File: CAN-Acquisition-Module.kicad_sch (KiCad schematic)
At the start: 0 parts

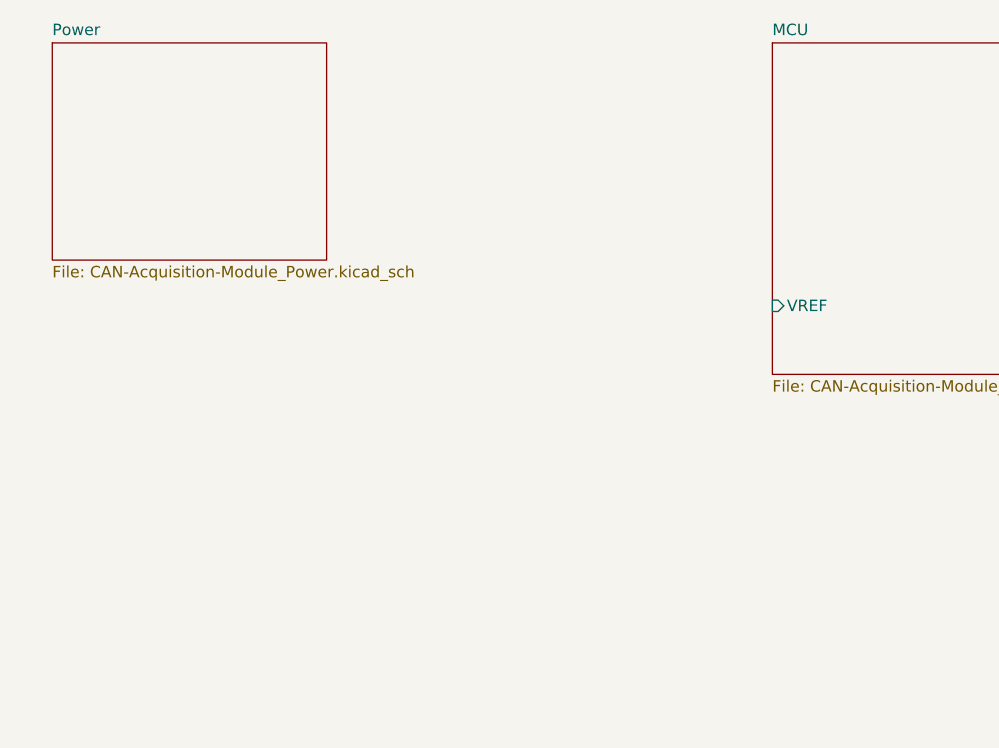
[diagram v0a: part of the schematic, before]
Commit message: Added CAN page
also power section has advanced
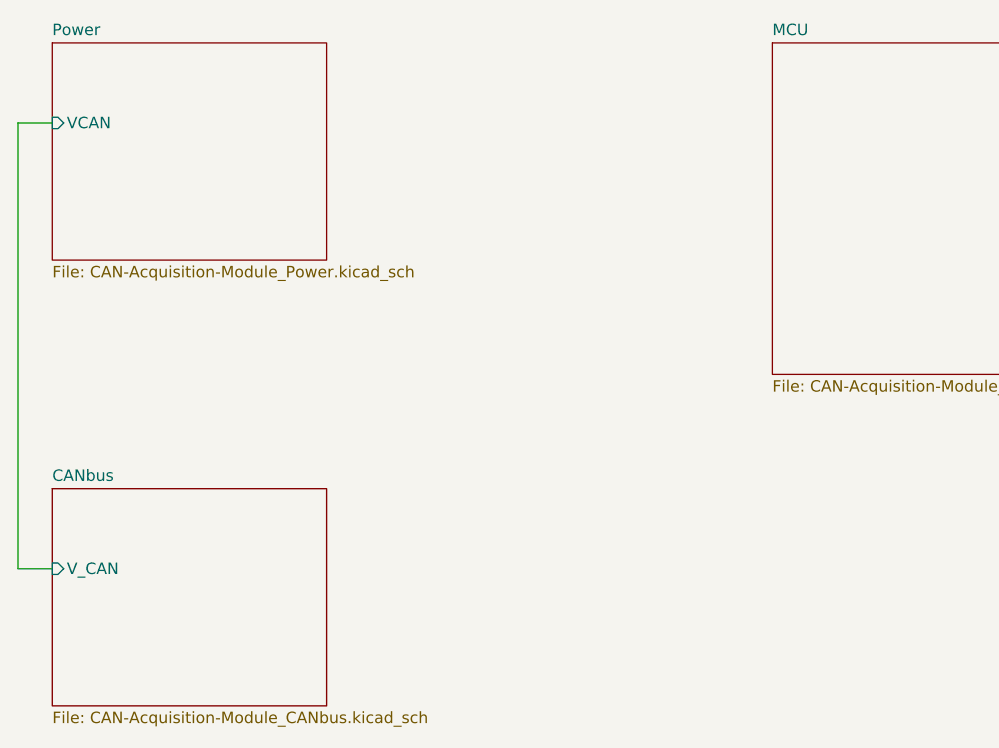
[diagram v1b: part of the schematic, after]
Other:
- added sheet CANbus (CAN-Acquisition-Module_CANbus.kicad_sch)
- sheet MCU ports: added none; removed VREF
- sheet Power ports: added VCAN; removed none

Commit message: Mid-day backup
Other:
- sheet MCU ports: added V_USB; removed none
- sheet Power ports: added V_CAN, V_USB; removed VCAN
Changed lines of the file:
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@@
 (kicad_sch (version 20211123) (generator eeschema)
   (paper "A4")
+  (wire (pts (xy 123.19 48.26) (xy 96.52 48.26))
+    (stroke (width 0) (type default) (color 0 0 0 0))
+  )
   (wire (pts (xy 39.37 101.6) (xy 43.18 101.6))
     (stroke (width 0) (type default) (color 0 0 0 0))
   )
   (wire (pts (xy 43.18 52.07) (xy 39.37 52.07))
+    (stroke (width 0) (type default) (color 0 0 0 0))
+  )
+  (wire (pts (xy 96.52 46.99) (xy 73.66 46.99))
+    (stroke (width 0) (type default) (color 0 0 0 0))
+  )
+  (wire (pts (xy 96.52 48.26) (xy 96.52 46.99))
     (stroke (width 0) (type default) (color 0 0 0 0))
   )
@@
       (effects (font (size 1.27 1.27)) (justify left top))
     )
+    (pin "V_USB" input (at 123.19 48.26 180)
+      (effects (font (size 1.27 1.27)) (justify left))
+    )
   )
   (sheet (at 43.18 43.18) (size 30.48 24.13) (fields_autoplaced)
@@
       (effects (font (size 1.27 1.27)) (justify left top))
     )
-    (pin "VCAN" input (at 43.18 52.07 180)
+    (pin "V_CAN" input (at 43.18 52.07 180)
       (effects (font (size 1.27 1.27)) (justify left))
+    )
+    (pin "V_USB" input (at 73.66 46.99 0)
+      (effects (font (size 1.27 1.27)) (justify right))
     )
   )
@@
       (reference "#PWR?") (unit 1) (value "+3.3VA") (footprint "")
     )
+    (path "/00000000-0000-0000-0000-0000628fa103/a38a5452-85ed-4430-a87b-bb057f60819d"
+      (reference "#PWR?") (unit 1) (value "GND") (footprint "")
+    )
     (path "/00000000-0000-0000-0000-0000628fba98/a44a161f-59e8-4a07-bda9-a9f7ef5f0a45"
+      (reference "#PWR?") (unit 1) (value "GND") (footprint "")
+    )
+    (path "/00000000-0000-0000-0000-0000628fa103/b9203d8f-14b0-4cbc-9d0d-c6be62782233"
       (reference "#PWR?") (unit 1) (value "GND") (footprint "")
     )
@@
       (reference "J?") (unit 1) (value "Conn_01x04") (footprint "")
     )
+    (path "/00000000-0000-0000-0000-0000628fa103/66fe8a96-0dd2-4c17-94e0-ac0305a23d19"
+      (reference "J?") (unit 1) (value "USB_B_Micro") (footprint "Connector_USB:USB_Micro-B_Wuerth_614105150721_Vertical")
+    )
     (path "/6a23b5b9-2864-4994-bd7a-8563b9182093/e692e733-abc9-4f31-850d-d3f34da81bc0"
       (reference "J?") (unit 1) (value "Conn_01x04") (footprint "")
@@
       (reference "L?") (unit 1) (value "Ferrite") (footprint "Inductor_SMD:L_0603_1608Metric")
     )
+    (path "/00000000-0000-0000-0000-0000628fa103/e13e828c-9966-43c1-9e8d-05ac776c208b"
+      (reference "L?") (unit 1) (value "Ferrite") (footprint "Inductor_SMD:L_0603_1608Metric")
+    )
     (path "/00000000-0000-0000-0000-0000628fba98/f1815cfb-946b-45e1-985b-8e0ed5e489f3"
       (reference "L?") (unit 1) (value "L_Iron_Small") (footprint "Inductor_SMD:L_1008_2520Metric")
@@
       (reference "R?") (unit 1) (value "100 Ω") (footprint "Resistor_SMD:R_0805_2012Metric")
     )
+    (path "/00000000-0000-0000-0000-0000628fa103/63402ccd-069c-4869-9df8-0a8a51225b07"
+      (reference "R?") (unit 1) (value "27 Ω") (footprint "Resistor_SMD:R_0603_1608Metric")
+    )
     (path "/00000000-0000-0000-0000-0000628fba98/bb37d496-e761-4ef3-bef0-688ba9e9bb7c"
       (reference "R?") (unit 1) (value "15 kΩ") (footprint "Resistor_SMD:R_0603_1608Metric")
@@
       (reference "R?") (unit 1) (value "47 kΩ") (footprint "Resistor_SMD:R_0603_1608Metric")
     )
+    (path "/00000000-0000-0000-0000-0000628fa103/f4f8312b-4abb-4eb0-aea9-7d0522332e6f"
+      (reference "R?") (unit 1) (value "27 Ω") (footprint "Resistor_SMD:R_0603_1608Metric")
+    )
     (path "/00000000-0000-0000-0000-0000628fa103/00000000-0000-0000-0000-0000628f5983"

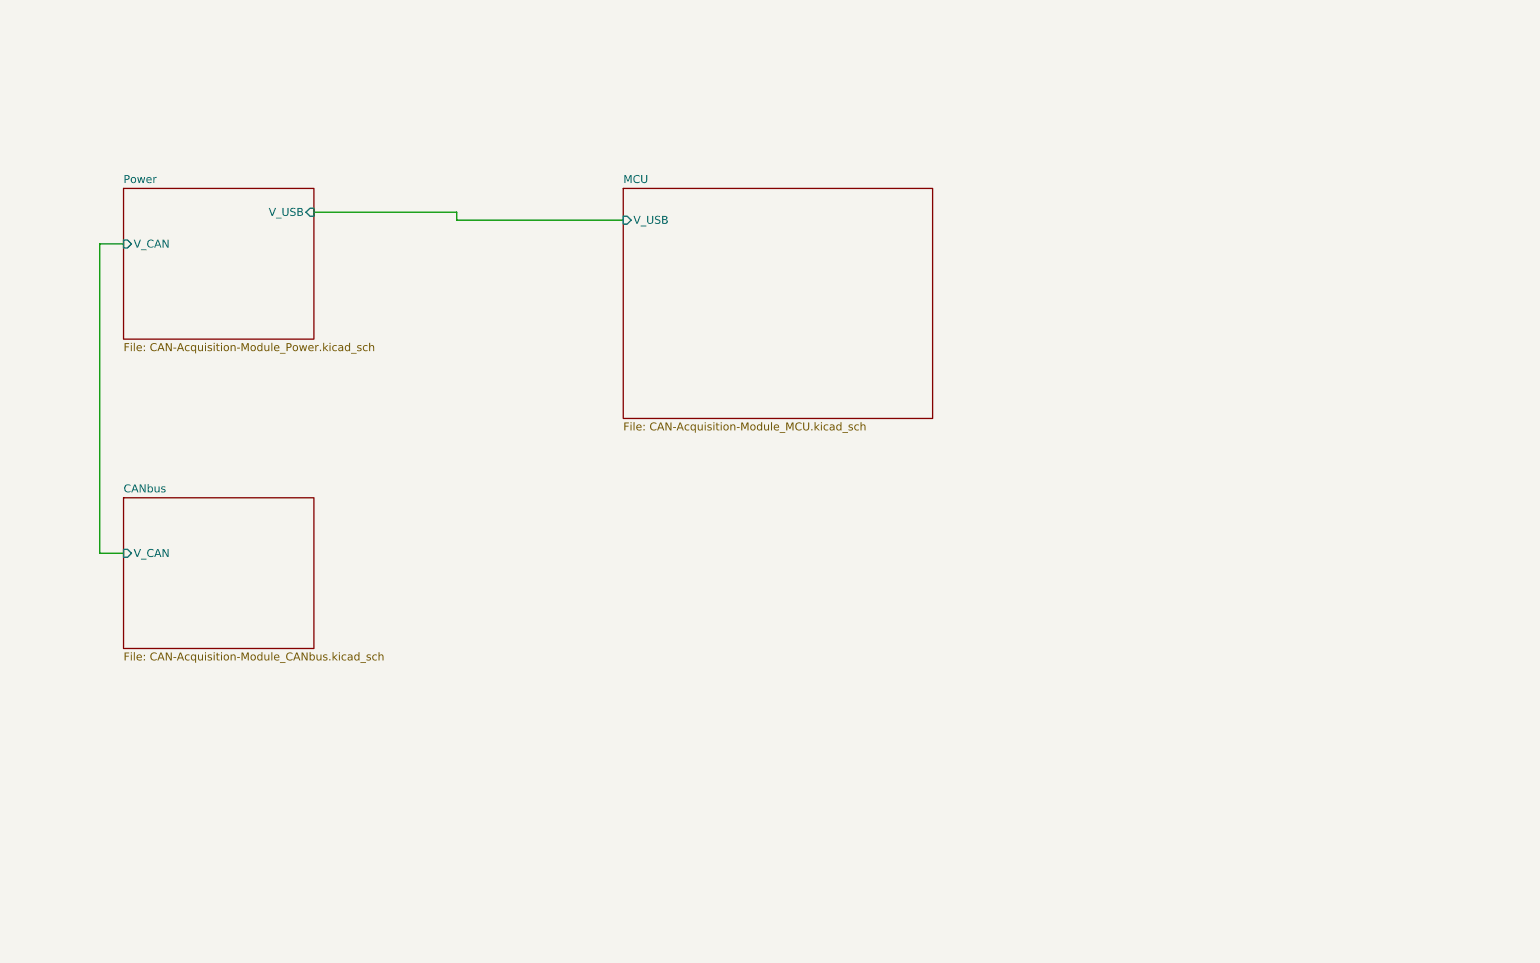
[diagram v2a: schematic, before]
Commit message: Advanced CAN section and "finished" power section
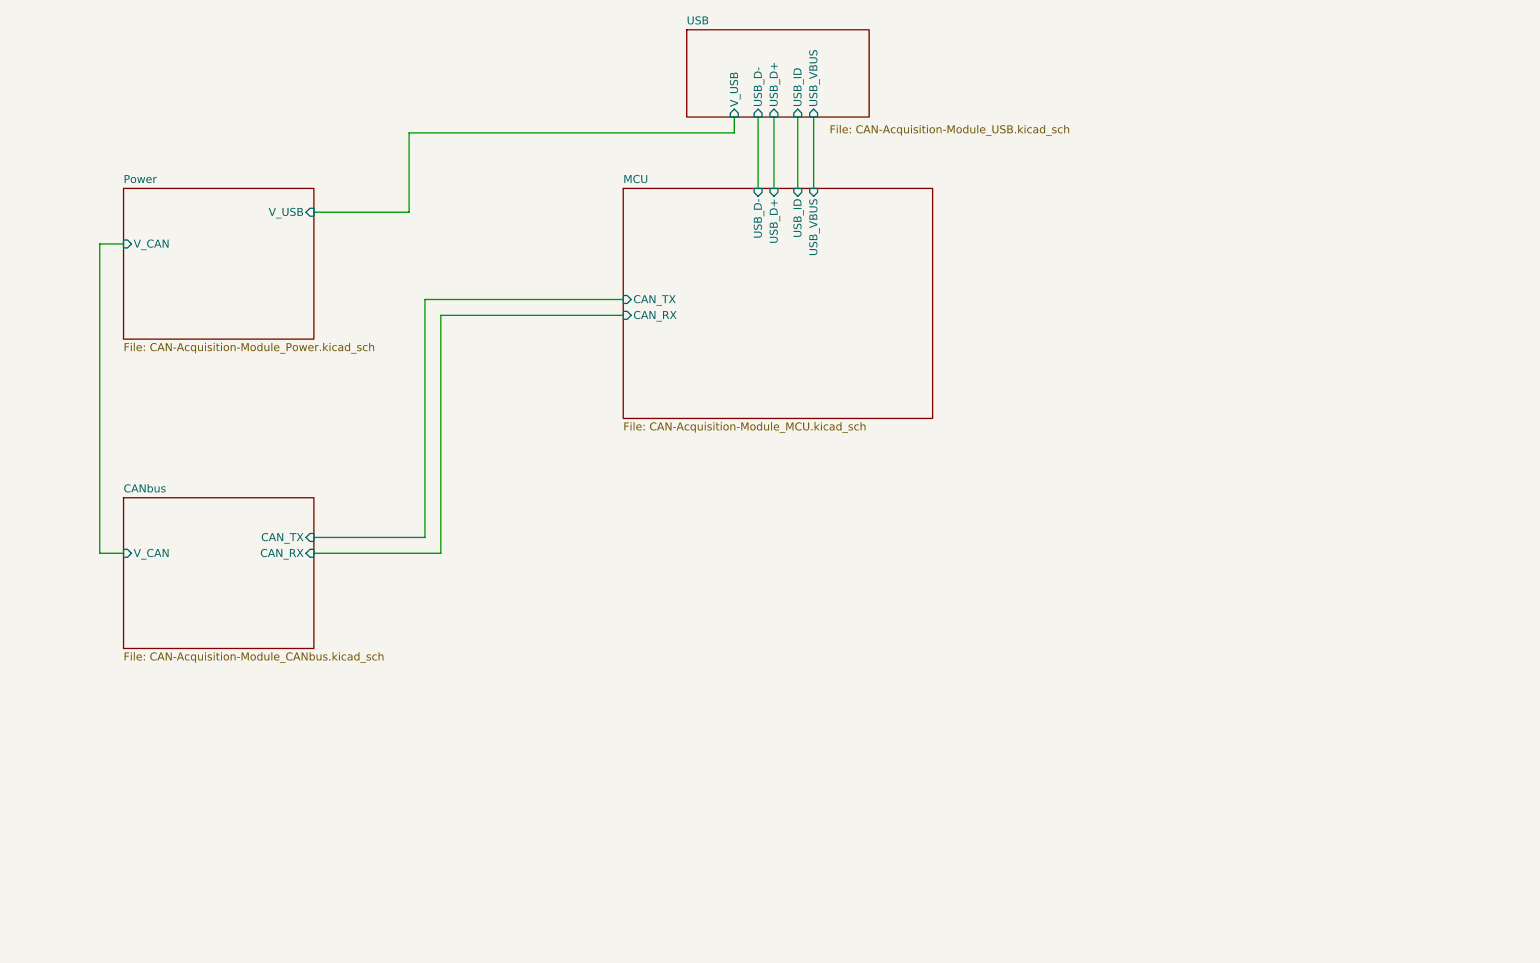
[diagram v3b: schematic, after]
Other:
- added sheet USB (CAN-Acquisition-Module_USB.kicad_sch)
- sheet CANbus ports: added CAN_RX, CAN_TX; removed none
- sheet MCU ports: added CAN_RX, CAN_TX, USB_D+, USB_D-, USB_ID, USB_VBUS; removed V_USB
